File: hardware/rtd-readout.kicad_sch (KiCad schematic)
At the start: 20 parts, among them J1 Conn_RTD_4W, J4 Conn_T7_Analog, J5 Conn_T7_I2C, J6 Conn_Power, U1 ADS1115IDGS (0x48), U2 ADS1115IDGS (0x49)

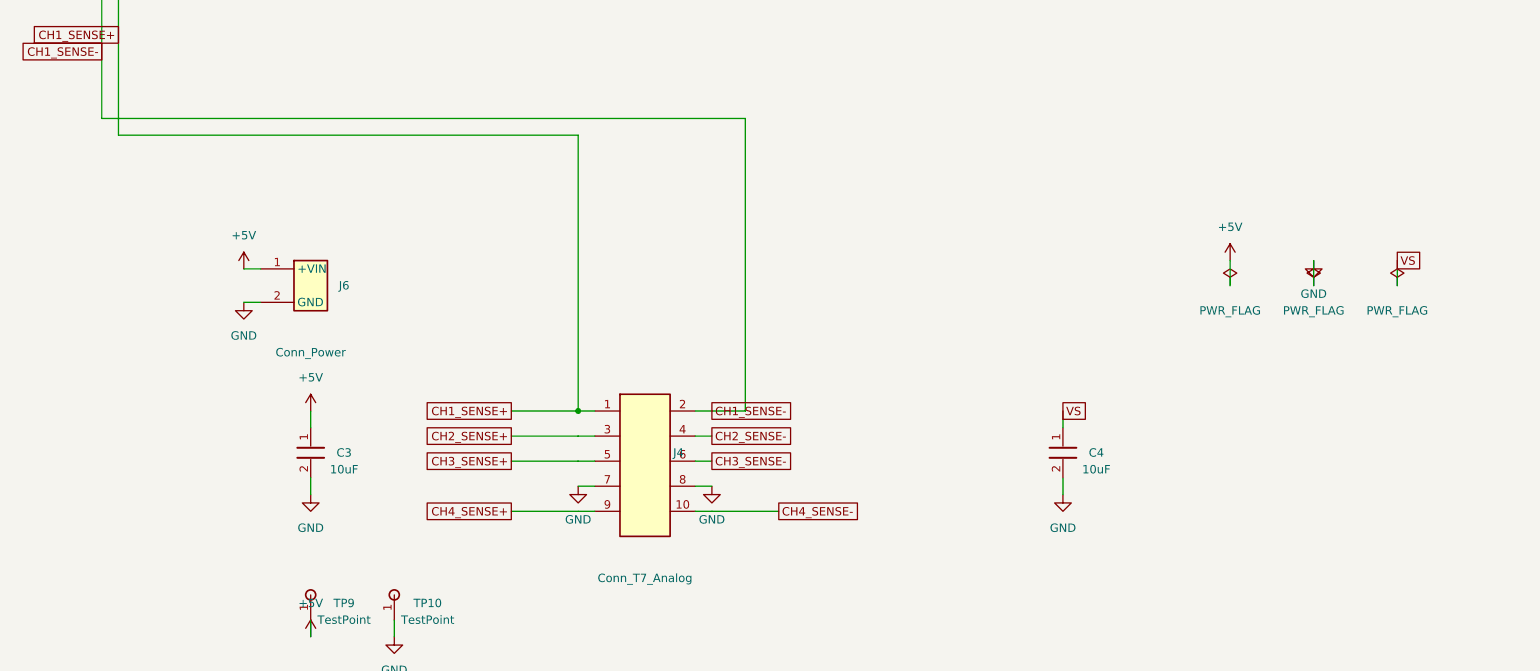
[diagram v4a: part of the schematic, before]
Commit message: rev-D: sense-line RC filters fitted (1k per leg + 0.1uF diff at J4, x4 ch)
Schematic: R7-R14 inline in CHn_SENSE+/- + C5-C8 differential; filtered nets
CHn_T7+/- labeled; netlist delta = exactly the filter insertion (23->31 nets,
oracle mutation-tested). Layout: Rs inline in existing legs (F-inline or
via-sandwich), caps on B.Cu across J4 pin pairs (courtyard-less variant);
ERC 0/0, DRC 0/0/0 (parity 84 metadata-only, 0 net conflicts); adversarial
copper review: all 8 filters genuinely in series, min clearance 0.315mm,
GND tie untouched. SPICE 7/7 - test5 now models fitted hardware. Fleet
visual findings fixed (text de-stacking, label moves, silk offsets, zero-
length residue). Closes the Session-006 open decision (USER_MANUAL 8.5).

Co-Authored-By: Claude Opus 4.8 <noreply@anthropic.com>
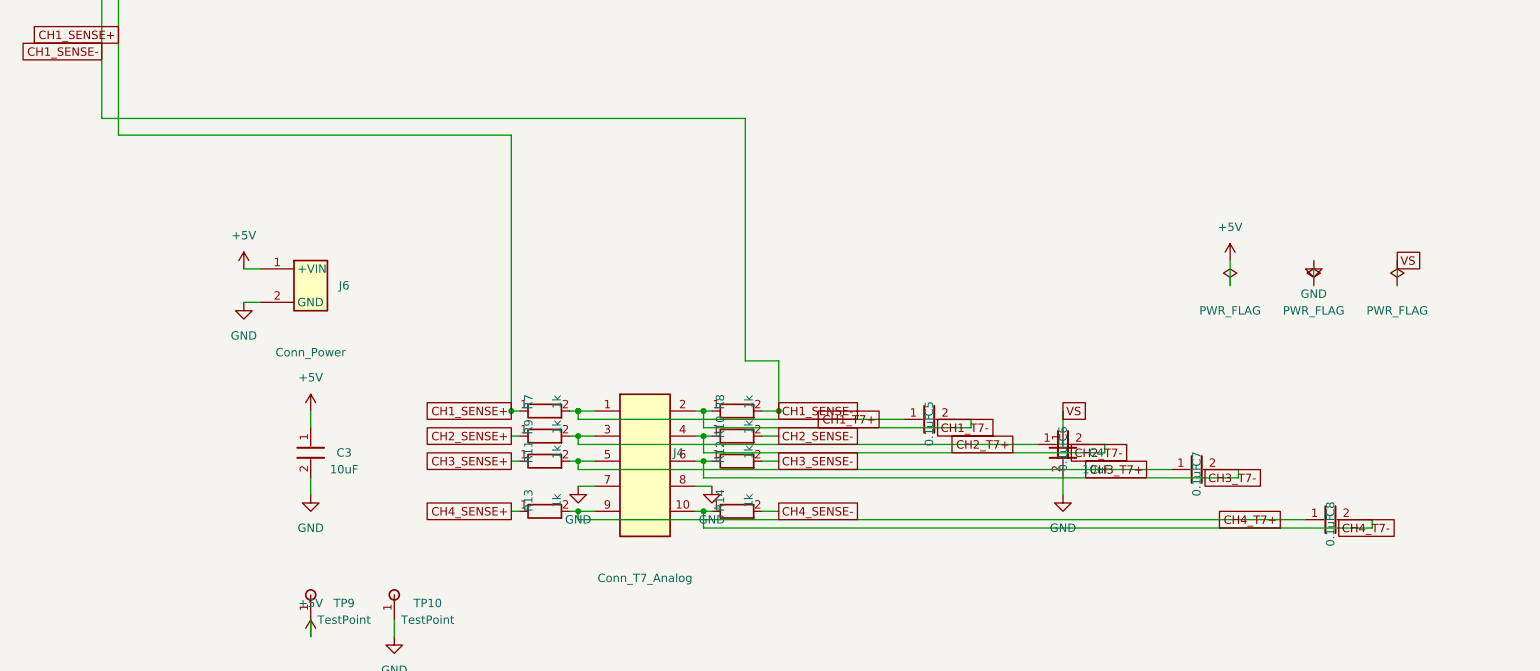
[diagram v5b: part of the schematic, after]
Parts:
- added C5, C6, C7, C8: 0.1uF, rtd-readout:C_0603_1608Metric, symbol rtd-readout:C
- added R10, R11, R12, R13, R14, R7, R8, R9: 1k, rtd-readout:R_0805_2012Metric, symbol rtd-readout:R
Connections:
- net CH1_SENSE+: now also R7.1; no longer J4.1 (CH1_Sense+)
- net CH1_SENSE-: now also R8.2; no longer J4.2 (CH1_Sense-)
- net CH2_SENSE+: now also R9.1; no longer J4.3 (CH2_Sense+)
- net CH2_SENSE-: now also R10.2; no longer J4.4 (CH2_Sense-)
- net CH3_SENSE+: now also R11.1; no longer J4.5 (CH3_Sense+)
- net CH3_SENSE-: now also R12.2; no longer J4.6 (CH3_Sense-)
- net CH4_SENSE+: now also R13.1; no longer J4.9 (CH4_Sense+)
- net CH4_SENSE-: now also R14.2; no longer J4.10 (CH4_Sense-)
- new net CH1_T7+: C5.1, J4.1 (CH1_Sense+), R7.2
- new net CH1_T7-: C5.2, J4.2 (CH1_Sense-), R8.1
- new net CH2_T7+: C6.1, J4.3 (CH2_Sense+), R9.2
- new net CH2_T7-: C6.2, J4.4 (CH2_Sense-), R10.1
- new net CH3_T7+: C7.1, J4.5 (CH3_Sense+), R11.2
- new net CH3_T7-: C7.2, J4.6 (CH3_Sense-), R12.1
- new net CH4_T7+: C8.1, J4.9 (CH4_Sense+), R13.2
- new net CH4_T7-: C8.2, J4.10 (CH4_Sense-), R14.1

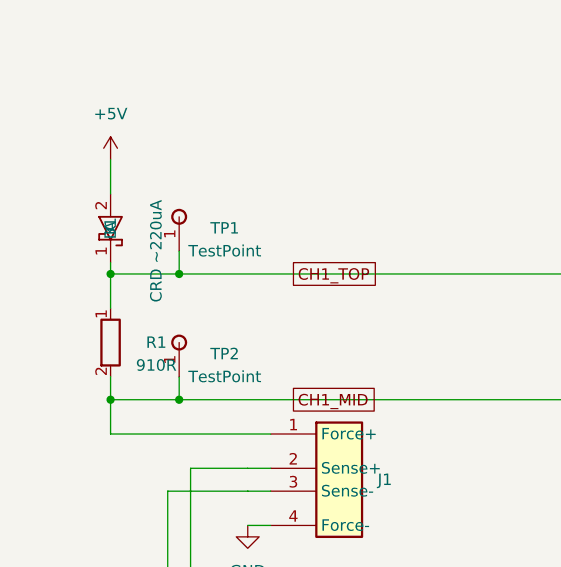
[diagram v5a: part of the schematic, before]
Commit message: rev-E: DFM/availability respin - CRD J500 TO-92, 0805 caps, R_ref 820R
Hand-assembly + live-Digi-Key-verified changes (all adversarially fact-checked):
- D1-D4: CDLL5283 MELF (unbuyable, 0 stock/40wk MOQ) -> LIS J500 TO-92 2L;
  new mirrored footprint TO-92-2_CRD-J500 (pad1=K at flat-to-silk insertion,
  0.8mm drill), 8 F.Cu stubs bridge old MELF trace ends to the THT pads.
- C1-C8: 0603 -> 0805 (Samsung CL21B104KBCNNNC / CL21A106KACLRNC; old Murata
  parts obsolete/backordered). C5-C8 keep the back-side across-J4 scheme.
- R_ref: 910R -> 820R (KOA RN73H2BTTD8200B10, 0.1%, 10ppm/C) - J500 band is
  +/-20%, 910R would clip the ADS1115 +/-0.256V range at band max.
- SPICE harness re-pointed (240uA, 820R, VL 1.2V, Z 4Meg; test4 gate <95% FS
  at kc=1.2); docs/spec/BOM_REVIEW/host defaults updated.

Gates: ERC 0/0, DRC 0 violations / 0 unconnected, SPICE 7/7 PASS
(t4: V_ref at band max = 237 mV = 93% FS, 14.9 bits).

Co-Authored-By: Claude Fable 5 <noreply@anthropic.com>
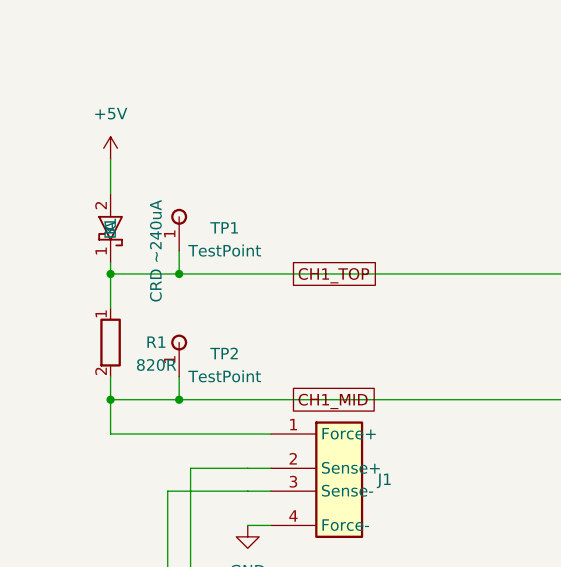
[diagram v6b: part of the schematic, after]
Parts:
- C1, C2, C5, C6, C7, C8: footprint rtd-readout:C_0603_1608Metric -> rtd-readout:C_0805_2012Metric; MPN GRM188R71H104KA93D -> CL21B104KBCNNNC; Manufacturer Murata -> Samsung Electro-Mechanics
- C3, C4: footprint rtd-readout:C_0603_1608Metric -> rtd-readout:C_0805_2012Metric; MPN GRM188R61E106KA73D -> CL21A106KACLRNC; Manufacturer Murata -> Samsung Electro-Mechanics
- D1: value CRD ~220uA -> CRD ~240uA; footprint rtd-readout:D_MELF -> rtd-readout:TO-92-2_CRD-J500; Current_nom ~0.22 mA (1N5283), +/-10%; stability over one scan is what 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 -> ~0.24 mA (J500), +/-20% band (0.192-0.288 mA); stability ov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; MPN CDLL5283 -> J500 TO-92 2L; Manufacturer Microchip (Microsemi / ex-Central Semiconductor) -> Linear Integrated Systems; Polarity Pin 1 = K (cathode, banded end). Pin 2 = A (anode). Matches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 -> Pin 1 = K (cathode). Pin 2 = A (anode). J500 TO-92 physical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
- R1: value 910R -> 820R; MPN TNPU1206 910R 0.1% 10ppm (confirm code) -> RN73H2BTTD8200B10
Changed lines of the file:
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@@
 			)
 		)
-		(property "Value" "CRD ~220uA"
+		(property "Value" "CRD ~240uA"
 			(at 43.18 48.26 0)
 			(show_name no)
@@
 			)
 		)
-		(property "Footprint" "rtd-readout:D_MELF"
+		(property "Footprint" "rtd-readout:TO-92-2_CRD-J500"
 			(at 38.1 45.72 0)
 			(show_name no)
@@
 			)
 		)
-		(property "Datasheet" "https://www.microchip.com/en-us/product/cdll5283-current-regulator-diode"
+		(property "Datasheet" "https://www.linearsystems.com/currentregulatingdiodes/j500-series"
 			(at 38.1 45.72 0)
 			(show_name no)
@@
 			)
 		)
-		(property "Description" "Current-regulator diode (constant-current diode), ~0.22 mA, two-terminal, DO-213AB MELF. Sets the per-channel excitation current; exact value is measured live and cancels (board_spec.md). Anode -> +V rail, cathode -> R_ref."
+		(property "Description" "Current-regulator diode (constant-current diode), ~0.24 mA (LIS J500, 0.192-0.288 mA band), two-terminal, TO-92 2-lead THT. Sets the per-channel excitation current; exact value is measured live and cancels (board_spec.md). Anode -> +V rail, cathode -> R_ref."
 			(at 38.1 45.72 0)
 			(show_name no)
@@
 			)
 		)
-		(property "MPN" "CDLL5283"
+		(property "MPN" "J500 TO-92 2L"
 			(at 38.1 45.72 0)
 			(show_name no)
@@
 			)
 		)
-		(property "Manufacturer" "Microchip (Microsemi / ex-Central Semiconductor)"
+		(property "Manufacturer" "Linear Integrated Systems"
 			(at 38.1 45.72 0)
 			(show_name no)
@@
 			)
 		)
-		(property "Polarity" "Pin 1 = K (cathode, banded end). Pin 2 = A (anode). Matches D_MELF pad 1 = cathode."
+		(property "Polarity" "Pin 1 = K (cathode). Pin 2 = A (anode). J500 TO-92 physical: facing the flat/marked face, left lead = A, right lead = K; the TO-92-2_CRD-J500 footprint silk is mirrored so matching the flat face to the silk outline puts K in pad 1."
 			(at 38.1 45.72 0)
 			(show_name no)
@@
 			)
 		)
-		(property "Current_nom" "~0.22 mA (1N5283), +/-10%; stability over one scan is what matters, not absolute value."
+		(property "Current_nom" "~0.24 mA (J500), +/-20% band (0.192-0.288 mA); stability over one scan is what matters, not absolute value."
 			(at 38.1 45.72 0)
 			(show_name no)
@@
 			)
 		)
-		(property "ki_keywords" "CRD current regulator diode constant current 1N5283 CDLL5283 RTD excitation MELF"
+		(property "ki_keywords" "CRD current regulator diode constant current J500 RTD excitation TO-92"
 			(at 38.1 45.72 0)
 			(show_name no)
@@
 			)
 		)
-		(property "ki_fp_filters" "D*MELF*"
+		(property "ki_fp_filters" "TO?92*"
 			(at 38.1 45.72 0)
 			(show_name no)
@@
 			)
 		)
-		(property "Value" "910R"
+		(property "Value" "820R"
 			(at 43.18 60.96 0)
 			(show_name no)
@@
 			)
 		)
-		(property "Datasheet" "https://www.susumu.co.jp/common/pdf/n_catalog_partition06_en.pdf"
+		(property "Datasheet" "https://www.koaspeer.com/pdfs/RN73H.pdf"
 			(at 38.1 58.42 0)
 			(show_name no)
@@
 			)
 		)
-		(property "Description" "Reference resistor for ratiometric current sense. ~910 ohm sets V_ref ~200 mV nominal inside the ADS1115 +/-0.256 V range. BINDING SPEC = tempco/stability, NOT absolute value (cross-cal constant C absorbs the value; board_spec.md s.R_ref)."
+		(property "Description" "Reference resistor for ratiometric current sense. 820 ohm sets V_ref ~197 mV nominal, <=236 mV at the J500 guaranteed-max 0.288 mA, inside the ADS1115 +/-0.256 V range. BINDING SPEC = tempco/stability, NOT absolute value (cross-cal constant C absorbs the value; board_spec.md s.R_ref)."
 			(at 38.1 58.42 0)
 			(show_name no)
@@
 			)
 		)
-		(property "MPN" "TNPU1206 910R 0.1% 10ppm (confirm code)"
+		(property "MPN" "RN73H2BTTD8200B10"
 			(at 38.1 58.42 0)
 			(show_name no)
@@
 			)
 		)
-		(property "Footprint" "rtd-readout:C_0603_1608Metric"
+		(property "Footprint" "rtd-readout:C_0805_2012Metric"
 			(at 184.15 78.74 0)
 			(show_name no)
@@
 			)
 		)
-		(property "Description" "Generic non-polarized chip capacitor, 0603. Use for per-ADS1115 VDD decoupling (0.1 uF) and general bypass."
+		(property "Description" "Generic non-polarized chip capacitor, 0805. Use for per-ADS1115 VDD decoupling (0.1 uF) and general bypass."
 			(at 184.15 78.74 0)
 			(show_name no)
@@
 			)
 		)
-		(property "MPN" "GRM188R71H104KA93D"
+		(property "MPN" "CL21B104KBCNNNC"
 			(at 184.15 78.74 0)
 			(show_name no)
@@
 			)
 		)
-		(property "Manufacturer" "Murata"
+		(property "Manufacturer" "Samsung Electro-Mechanics"
 			(at 184.15 78.74 0)
 			(show_name no)
@@
 			)
 		)
-		(property "Footprint" "rtd-readout:C_0603_1608Metric"
+		(property "Footprint" "rtd-readout:C_0805_2012Metric"
 			(at 209.55 78.74 0)
 			(show_name no)
@@
 			)
 		)
-		(property "Description" "Generic non-polarized chip capacitor, 0603. Use for per-ADS1115 VDD decoupling (0.1 uF) and general bypass."
+		(property "Description" "Generic non-polarized chip capacitor, 0805. Use for per-ADS1115 VDD decoupling (0.1 uF) and general bypass."
 			(at 209.55 78.74 0)
 			(show_name no)
@@
 			)
 		)
-		(property "MPN" "GRM188R71H104KA93D"
+		(property "MPN" "CL21B104KBCNNNC"
 			(at 209.55 78.74 0)
 			(show_name no)
@@
 			)
 		)
-		(property "Manufacturer" "Murata"
+		(property "Manufacturer" "Samsung Electro-Mechanics"
 			(at 209.55 78.74 0)
 			(show_name no)
@@
 			)
 		)
-		(property "Footprint" "rtd-readout:C_0603_1608Metric"
+		(property "Footprint" "rtd-readout:C_0805_2012Metric"
 			(at 76.2 165.1 0)
 			(show_name no)
@@
 			)
 		)
-		(property "Description" "Generic non-polarized chip capacitor, 0603. Use for per-ADS1115 VDD decoupling (0.1 uF) and general bypass."
+		(property "Description" "Generic non-polarized chip capacitor, 0805. Use for per-ADS1115 VDD decoupling (0.1 uF) and general bypass."
 			(at 76.2 165.1 0)
 			(show_name no)
@@
 			)
 		)
-		(property "MPN" "GRM188R61E106KA73D"
+		(property "MPN" "CL21A106KACLRNC"
 			(at 76.2 165.1 0)
 			(show_name no)
@@
 			)
 		)
-		(property "Manufacturer" "Murata"
+		(property "Manufacturer" "Samsung Electro-Mechanics"
 			(at 76.2 165.1 0)
 			(show_name no)
@@
 			)
 		)
-		(property "Footprint" "rtd-readout:C_0603_1608Metric"
+		(property "Footprint" "rtd-readout:C_0805_2012Metric"
 			(at 190.5 165.1 0)
 			(show_name no)
@@
 			)
 		)
-		(property "Description" "Generic non-polarized chip capacitor, 0603. Use for per-ADS1115 VDD decoupling (0.1 uF) and general bypass."
+		(property "Description" "Generic non-polarized chip capacitor, 0805. Use for per-ADS1115 VDD decoupling (0.1 uF) and general bypass."
 			(at 190.5 165.1 0)
 			(show_name no)
@@
 			)
 		)
-		(property "MPN" "GRM188R61E106KA73D"
+		(property "MPN" "CL21A106KACLRNC"
 			(at 190.5 165.1 0)
 			(show_name no)
@@
 			)
 		)
-		(property "Manufacturer" "Murata"
+		(property "Manufacturer" "Samsung Electro-Mechanics"
 			(at 190.5 165.1 0)
 			(show_name no)
@@
 			)
 		)
-		(property "Footprint" "rtd-readout:C_0603_1608Metric"
+		(property "Footprint" "rtd-readout:C_0805_2012Metric"
 			(at 176.53 160.02 0)
 			(show_name no)
@@
 			)
 		)
-		(property "Description" "Generic non-polarized chip capacitor, 0603. Use for per-ADS1115 VDD decoupling (0.1 uF) and general bypass."
+		(property "Description" "Generic non-polarized chip capacitor, 0805. Use for per-ADS1115 VDD decoupling (0.1 uF) and general bypass."
 			(at 176.53 160.02 0)
 			(show_name no)
@@
 			)
 		)
-		(property "MPN" "GRM188R71H104KA93D"
+		(property "MPN" "CL21B104KBCNNNC"
 			(at 176.53 160.02 0)
 			(show_name no)
@@
 			)
 		)
-		(property "Manufacturer" "Murata"
+		(property "Manufacturer" "Samsung Electro-Mechanics"
 			(at 176.53 160.02 0)
 			(show_name no)
@@
 			)
 		)
-		(property "Footprint" "rtd-readout:C_0603_1608Metric"
+		(property "Footprint" "rtd-readout:C_0805_2012Metric"
 			(at 176.53 163.83 0)
 			(show_name no)
@@
 			)
 		)
-		(property "Description" "Generic non-polarized chip capacitor, 0603. Use for per-ADS1115 VDD decoupling (0.1 uF) and general bypass."
+		(property "Description" "Generic non-polarized chip capacitor, 0805. Use for per-ADS1115 VDD decoupling (0.1 uF) and general bypass."
 			(at 176.53 163.83 0)
 			(show_name no)
@@
 			)
 		)
-		(property "MPN" "GRM188R71H104KA93D"
+		(property "MPN" "CL21B104KBCNNNC"
 			(at 176.53 163.83 0)
 			(show_name no)
@@
 			)
 		)
-		(property "Manufacturer" "Murata"
+		(property "Manufacturer" "Samsung Electro-Mechanics"
 			(at 176.53 163.83 0)
 			(show_name no)
@@
 			)
 		)
-		(property "Footprint" "rtd-readout:C_0603_1608Metric"
+		(property "Footprint" "rtd-readout:C_0805_2012Metric"
 			(at 176.53 167.64 0)
 			(show_name no)
@@
 			)
 		)
-		(property "Description" "Generic non-polarized chip capacitor, 0603. Use for per-ADS1115 VDD decoupling (0.1 uF) and general bypass."
+		(property "Description" "Generic non-polarized chip capacitor, 0805. Use for per-ADS1115 VDD decoupling (0.1 uF) and general bypass."
 			(at 176.53 167.64 0)
 			(show_name no)
@@
 			)
 		)
-		(property "MPN" "GRM188R71H104KA93D"
+		(property "MPN" "CL21B104KBCNNNC"
 			(at 176.53 167.64 0)
 			(show_name no)
@@
 			)
 		)
-		(property "Manufacturer" "Murata"
+		(property "Manufacturer" "Samsung Electro-Mechanics"
 			(at 176.53 167.64 0)
 			(show_name no)
@@
 			)
 		)
-		(property "Footprint" "rtd-readout:C_0603_1608Metric"
+		(property "Footprint" "rtd-readout:C_0805_2012Metric"
 			(at 176.53 175.26 0)
 			(show_name no)
@@
 			)
 		)
-		(property "Description" "Generic non-polarized chip capacitor, 0603. Use for per-ADS1115 VDD decoupling (0.1 uF) and general bypass."
+		(property "Description" "Generic non-polarized chip capacitor, 0805. Use for per-ADS1115 VDD decoupling (0.1 uF) and general bypass."
 			(at 176.53 175.26 0)
 			(show_name no)
@@
 			)
 		)
-		(property "MPN" "GRM188R71H104KA93D"
+		(property "MPN" "CL21B104KBCNNNC"
 			(at 176.53 175.26 0)
 			(show_name no)
@@
 			)
 		)
-		(property "Manufacturer" "Murata"
+		(property "Manufacturer" "Samsung Electro-Mechanics"
 			(at 176.53 175.26 0)
 			(show_name no)
